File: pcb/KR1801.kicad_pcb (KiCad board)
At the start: 2 copper layers, 1 part, among them U1 К1801ВМ1

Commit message: ECB
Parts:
- added J1: ECB, Connector_DIN:DIN41612_R_3x32_Male_Horizontal_THT, F.Cu at (216.3, 60.0)
- added MH1: MountingHole_2.7mm_M2.5_DIN965, MountingHole:MountingHole_2.7mm_M2.5_DIN965, F.Cu at (65.2, 55.0)
- added MH2: MountingHole_2.7mm_M2.5_DIN965, MountingHole:MountingHole_2.7mm_M2.5_DIN965, F.Cu at (65.2, 143.9)
- moved U1 21.8 mm to (134.4, 111.9), turned to 90 degrees
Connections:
- U1 pad 1: unconnected-(U1-CLC-Pad1) -> CLC
- U1 pad 21: unconnected-(U1-GND-Pad21) -> GND
- U1 pad 29: unconnected-(U1-~{DCLO}-Pad29) -> ~{DCLO}
- U1 pad 30: unconnected-(U1-~{ACLO}-Pad30) -> ~{ACLO}
- U1 pad 34: unconnected-(U1-~{INIT}-Pad34) -> ~{INIT}
- U1 pad 42: unconnected-(U1-VCC-Pad42) -> VCC
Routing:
- net VCC: track 0.00 -> 104.2 mm
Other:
- board outline added: 160 x 100 mm
- board text added: "Mounting holes are optional Keepout areas are for for guide rails"

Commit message: 3D models
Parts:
- moved U1 2.99 mm to (136.4, 109.8)
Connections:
- J1 pad a11: unconnected-(J1-Pin_a11-Pada11) -> ~{DMR}
- J1 pad a22: unconnected-(J1-Pin_a22-Pada22) -> ~{RPLY}
- J1 pad a31: unconnected-(J1-Pin_a31-Pada31) -> ~{DMGO}
- J1 pad b25: unconnected-(J1-Pin_b25-Padb25) -> ~{IAKO}
- J1 pad c21: unconnected-(J1-Pin_c21-Padc21) -> ~{VIRQ}
- J1 pad c22: unconnected-(J1-Pin_c22-Padc22) -> ~{DOUT}
- J1 pad c24: unconnected-(J1-Pin_c24-Padc24) -> ~{DIN}
- J1 pad c25: unconnected-(J1-Pin_c25-Padc25) -> ~{IRQ1}
- U1 pad 2: unconnected-(U1-~{SACK}-Pad2) -> ~{SACK}
- U1 pad 31: unconnected-(U1-~{IRQ1}-Pad31) -> ~{IRQ1}
- U1 pad 32: unconnected-(U1-IRQ2-Pad32) -> ~{IRQ2}
- U1 pad 33: unconnected-(U1-IRQ3-Pad33) -> ~{IRQ3}
- U1 pad 35: unconnected-(U1-VIRQ-Pad35) -> ~{VIRQ}
- U1 pad 36: unconnected-(U1-IAKO-Pad36) -> ~{IAKO}
- U1 pad 37: unconnected-(U1-~{DOUT}-Pad37) -> ~{DOUT}
- U1 pad 38: unconnected-(U1-~{DIN}-Pad38) -> ~{DIN}
- U1 pad 39: unconnected-(U1-~{RPLY}-Pad39) -> ~{RPLY}
- U1 pad 4: unconnected-(U1-~{DMGO}-Pad4) -> ~{DMGO}
- U1 pad 40: unconnected-(U1-~{WTBT}-Pad40) -> ~{WTBT}
- U1 pad 41: unconnected-(U1-~{SYNC}-Pad41) -> ~{ALE}
- U1 pad 5: unconnected-(U1-~{DMR}-Pad5) -> ~{DMR}
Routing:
- net VCC: track 104.2 -> 0.00 mm

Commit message: random placement test
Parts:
- added R1: R, Resistor_SMD:R_0603_1608Metric_Pad0.98x0.95mm_HandSolder, F.Cu at (135.0, 123.7)
- added R10: 0R, Resistor_SMD:R_0603_1608Metric_Pad0.98x0.95mm_HandSolder, F.Cu at (145.8, 72.4)
- added R11: 0R, Resistor_SMD:R_0603_1608Metric_Pad0.98x0.95mm_HandSolder, F.Cu at (140.0, 72.3)
- added R12: R, Resistor_SMD:R_0603_1608Metric_Pad0.98x0.95mm_HandSolder, F.Cu at (172.3, 59.4)
- added R13: R, Resistor_SMD:R_0603_1608Metric_Pad0.98x0.95mm_HandSolder, F.Cu at (143.0, 72.3)
- added R14: R, Resistor_SMD:R_0603_1608Metric_Pad0.98x0.95mm_HandSolder, F.Cu at (137.6, 72.3)
- added R15: R, Resistor_SMD:R_0603_1608Metric_Pad0.98x0.95mm_HandSolder, F.Cu at (132.2, 123.9)
- added R2: R, Resistor_SMD:R_0603_1608Metric_Pad0.98x0.95mm_HandSolder, F.Cu at (137.5, 123.7)
- added R3: R, Resistor_SMD:R_0603_1608Metric_Pad0.98x0.95mm_HandSolder, F.Cu at (139.8, 123.7)
- added R4: R, Resistor_SMD:R_0603_1608Metric_Pad0.98x0.95mm_HandSolder, F.Cu at (142.8, 123.7)
- added R5: R, Resistor_SMD:R_0603_1608Metric_Pad0.98x0.95mm_HandSolder, F.Cu at (145.1, 123.6)
- added R6: R, Resistor_SMD:R_0603_1608Metric_Pad0.98x0.95mm_HandSolder, F.Cu at (149.4, 72.3)
- added R7: R, Resistor_SMD:R_0603_1608Metric_Pad0.98x0.95mm_HandSolder, F.Cu at (147.0, 123.6)
- added R8: 0R, Resistor_SMD:R_0603_1608Metric_Pad0.98x0.95mm_HandSolder, F.Cu at (129.8, 123.8)
- added R9: 0R, Resistor_SMD:R_0603_1608Metric_Pad0.98x0.95mm_HandSolder, F.Cu at (127.6, 123.8)
- added U2: 74LS573, Package_SO:SOIC-20W_7.5x12.8mm_P1.27mm, F.Cu at (180.2, 80.8)
- added U3: 74LS573, Package_SO:SOIC-20W_7.5x12.8mm_P1.27mm, F.Cu at (180.8, 108.8)
- added U4: 74LS245, Package_SO:SOIC-20W_7.5x12.8mm_P1.27mm, F.Cu at (193.0, 65.4)
- added U5: 74LS245, Package_SO:SOIC-20W_7.5x12.8mm_P1.27mm, F.Cu at (193.2, 94.0)
- moved U1 29.0 mm to (150.6, 84.5), turned to -90 degrees
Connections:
- J1 pad a18: unconnected-(J1-A14-Pada18) -> A14
- J1 pad a2: unconnected-(J1-D5-Pada2) -> DB5
- J1 pad a29: unconnected-(J1-A13-Pada29) -> A13
- J1 pad a3: unconnected-(J1-D6-Pada3) -> DB6
- J1 pad a30: unconnected-(J1-A9-Pada30) -> A9
- J1 pad a4: unconnected-(J1-D3-Pada4) -> DB3
- J1 pad a5: unconnected-(J1-D4-Pada5) -> DB4
- J1 pad a6: unconnected-(J1-A2-Pada6) -> A2
- J1 pad a7: unconnected-(J1-A4-Pada7) -> A4
- J1 pad a8: unconnected-(J1-A5-Pada8) -> A5
- J1 pad a9: unconnected-(J1-A6-Pada9) -> A6
- J1 pad b10: unconnected-(J1-D12-Padb10) -> DB12
- J1 pad b11: unconnected-(J1-D13-Padb11) -> DB13
- J1 pad b12: unconnected-(J1-D14-Padb12) -> DB14
- J1 pad b13: unconnected-(J1-D15-Padb13) -> DB15
- J1 pad b6: unconnected-(J1-D8-Padb6) -> DB8
- J1 pad b7: unconnected-(J1-D9-Padb7) -> DB9
- J1 pad b8: unconnected-(J1-D10-Padb8) -> DB10
- J1 pad b9: unconnected-(J1-D11-Padb9) -> DB11
- J1 pad c14: unconnected-(J1-D1-Padc14) -> DB1
- J1 pad c17: unconnected-(J1-A11-Padc17) -> A11
- J1 pad c18: unconnected-(J1-A10-Padc18) -> A10
- J1 pad c2: unconnected-(J1-D0-Padc2) -> DB0
- J1 pad c20: ~{ACLO} -> ~{NMI}
- J1 pad c26: ~{INIT} -> ~{DCLO}
- J1 pad c27: unconnected-(J1-A12-Padc27) -> A12
- J1 pad c28: unconnected-(J1-A15-Padc28) -> A15
- J1 pad c3: unconnected-(J1-D7-Padc3) -> DB7
- J1 pad c4: unconnected-(J1-D2-Padc4) -> DB2
- J1 pad c5: unconnected-(J1-A0-Padc5) -> A0
- J1 pad c6: unconnected-(J1-A3-Padc6) -> A3
- J1 pad c7: unconnected-(J1-A1-Padc7) -> A1
- J1 pad c8: unconnected-(J1-A8-Padc8) -> A8
- J1 pad c9: unconnected-(J1-A7-Padc9) -> A7
- U1 pad 10: unconnected-(U1-AD1-Pad10) -> AD1
- U1 pad 11: unconnected-(U1-AD2-Pad11) -> AD2
- U1 pad 12: unconnected-(U1-AD3-Pad12) -> AD3
- U1 pad 13: unconnected-(U1-AD4-Pad13) -> AD4
- U1 pad 14: unconnected-(U1-AD5-Pad14) -> AD5
- U1 pad 15: unconnected-(U1-AD6-Pad15) -> AD6
- U1 pad 16: unconnected-(U1-AD7-Pad16) -> AD7
- U1 pad 17: unconnected-(U1-AD8-Pad17) -> AD8
- U1 pad 18: unconnected-(U1-AD9-Pad18) -> AD9
- U1 pad 19: unconnected-(U1-AD10-Pad19) -> AD10
- U1 pad 20: unconnected-(U1-AD11-Pad20) -> AD11
- U1 pad 22: unconnected-(U1-AD12-Pad22) -> AD12
- U1 pad 23: unconnected-(U1-AD13-Pad23) -> AD13
- U1 pad 24: unconnected-(U1-AD14-Pad24) -> AD14
- U1 pad 25: unconnected-(U1-AD15-Pad25) -> AD15
- U1 pad 26: (no net) -> Net-(U1-~{PA1})
- U1 pad 27: unconnected-(U1-Pad27) -> Net-(U1-~{PA0})
- U1 pad 28: unconnected-(U1-Pad28) -> AB.OE
- U1 pad 3: unconnected-(U1-Pad3) -> Net-(U1-~{DMGI})
- U1 pad 34: ~{INIT} -> ~{DCLO}
- U1 pad 6: unconnected-(U1-Pad6) -> Net-(U1-~{SP})
- U1 pad 7: unconnected-(U1-SEL1-Pad7) -> ~{SEL1}
- U1 pad 8: unconnected-(U1-SEL2-Pad8) -> ~{SEL2}
- U1 pad 9: unconnected-(U1-AD0-Pad9) -> AD0

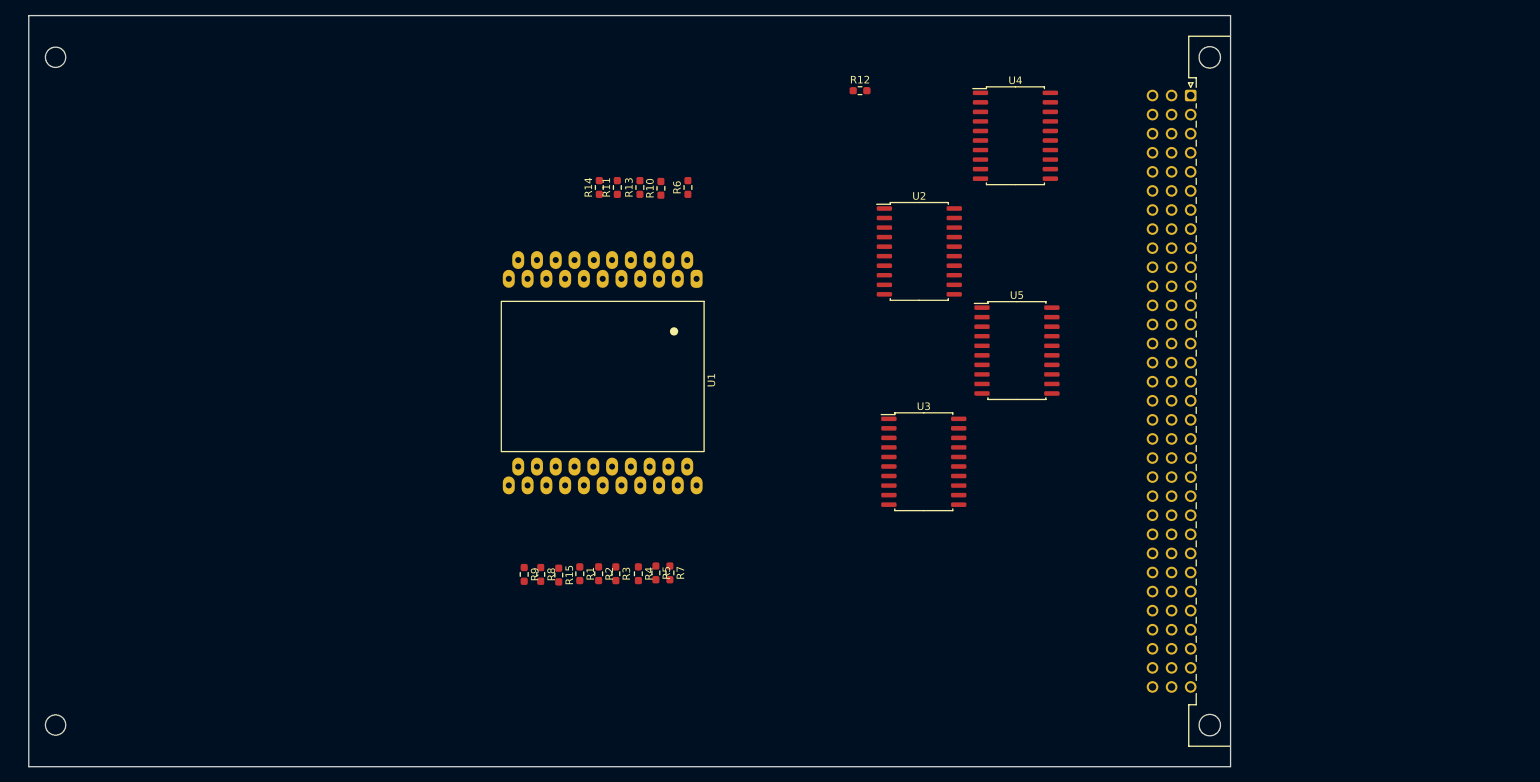
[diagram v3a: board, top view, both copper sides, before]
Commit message: most of the glue logic and controls
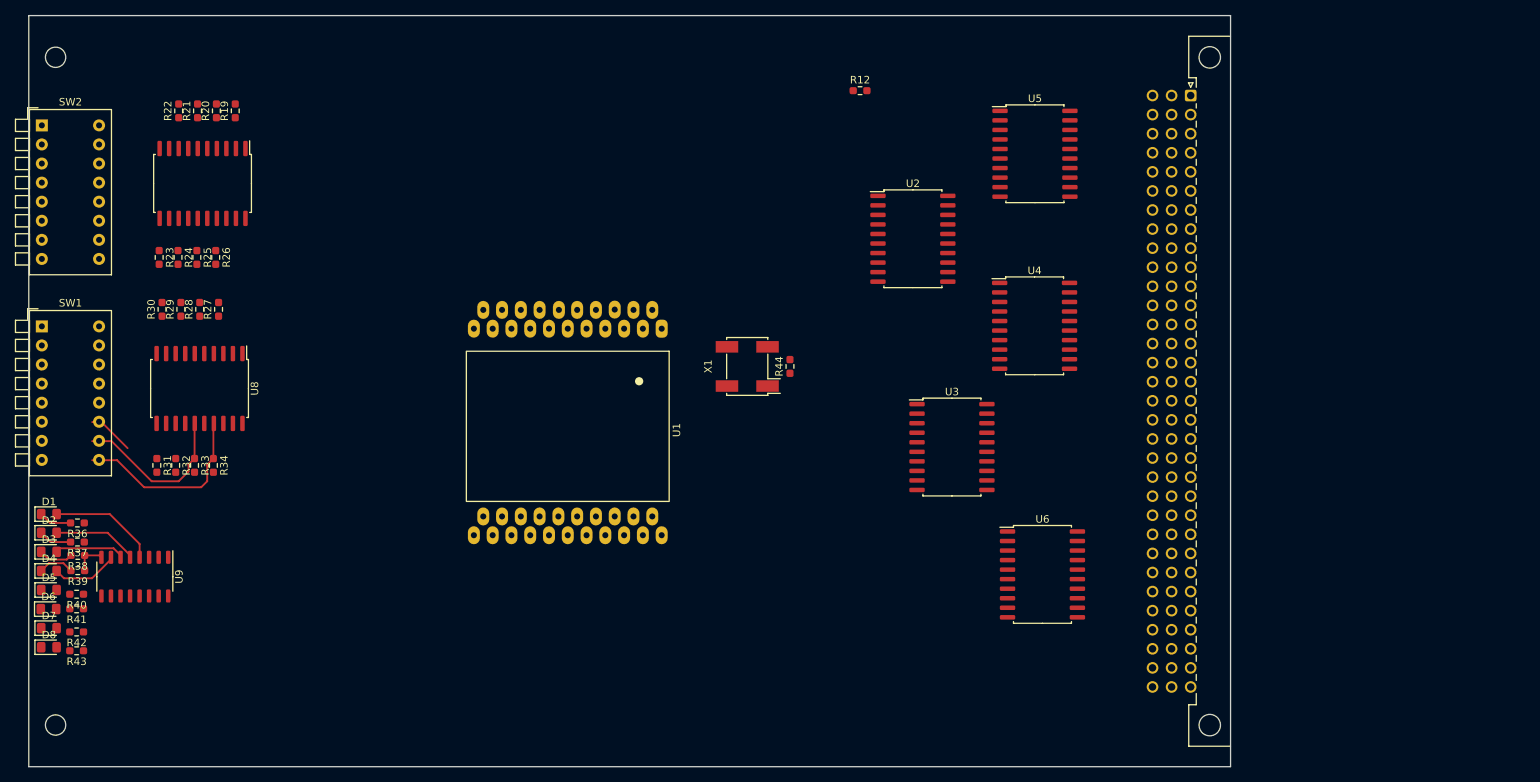
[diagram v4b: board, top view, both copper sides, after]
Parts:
- removed R1, R13, R14, R15, R2, R3, R4, R5, R6, R7: R, Resistor_SMD:R_0603_1608Metric_Pad0.98x0.95mm_HandSolder
- removed R10, R11, R8, R9: 0R, Resistor_SMD:R_0603_1608Metric_Pad0.98x0.95mm_HandSolder
- added D1: LED, LED_SMD:LED_0805_2012Metric_Pad1.15x1.40mm_HandSolder, F.Cu at (64.3, 115.8)
- added D2: LED, LED_SMD:LED_0805_2012Metric_Pad1.15x1.40mm_HandSolder, F.Cu at (64.3, 118.3)
- added D3: LED, LED_SMD:LED_0805_2012Metric_Pad1.15x1.40mm_HandSolder, F.Cu at (64.3, 120.8)
- added D4: LED, LED_SMD:LED_0805_2012Metric_Pad1.15x1.40mm_HandSolder, F.Cu at (64.3, 123.3)
- added D5: LED, LED_SMD:LED_0805_2012Metric_Pad1.15x1.40mm_HandSolder, F.Cu at (64.3, 125.9)
- added D6: LED, LED_SMD:LED_0805_2012Metric_Pad1.15x1.40mm_HandSolder, F.Cu at (64.3, 128.4)
- added D7: LED, LED_SMD:LED_0805_2012Metric_Pad1.15x1.40mm_HandSolder, F.Cu at (64.3, 131.0)
- added D8: LED, LED_SMD:LED_0805_2012Metric_Pad1.15x1.40mm_HandSolder, F.Cu at (64.3, 133.5)
- added R19: R, Resistor_SMD:R_0603_1608Metric_Pad0.98x0.95mm_HandSolder, F.Cu at (89.1, 62.1)
- added R20: R, Resistor_SMD:R_0603_1608Metric_Pad0.98x0.95mm_HandSolder, F.Cu at (86.6, 62.1)
- added R21: R, Resistor_SMD:R_0603_1608Metric_Pad0.98x0.95mm_HandSolder, F.Cu at (84.1, 62.1)
- added R22: R, Resistor_SMD:R_0603_1608Metric_Pad0.98x0.95mm_HandSolder, F.Cu at (81.6, 62.1)
- added R23: R, Resistor_SMD:R_0603_1608Metric_Pad0.98x0.95mm_HandSolder, F.Cu at (79.0, 81.6)
- added R24: R, Resistor_SMD:R_0603_1608Metric_Pad0.98x0.95mm_HandSolder, F.Cu at (81.5, 81.6)
- added R25: R, Resistor_SMD:R_0603_1608Metric_Pad0.98x0.95mm_HandSolder, F.Cu at (84.0, 81.6)
- added R26: R, Resistor_SMD:R_0603_1608Metric_Pad0.98x0.95mm_HandSolder, F.Cu at (86.5, 81.6)
- added R27: R, Resistor_SMD:R_0603_1608Metric_Pad0.98x0.95mm_HandSolder, F.Cu at (86.9, 88.5)
- added R28: R, Resistor_SMD:R_0603_1608Metric_Pad0.98x0.95mm_HandSolder, F.Cu at (84.4, 88.5)
- added R29: R, Resistor_SMD:R_0603_1608Metric_Pad0.98x0.95mm_HandSolder, F.Cu at (81.9, 88.5)
- added R30: R, Resistor_SMD:R_0603_1608Metric_Pad0.98x0.95mm_HandSolder, F.Cu at (79.4, 88.5)
- added R31: R, Resistor_SMD:R_0603_1608Metric_Pad0.98x0.95mm_HandSolder, F.Cu at (78.7, 109.3)
- added R32: R, Resistor_SMD:R_0603_1608Metric_Pad0.98x0.95mm_HandSolder, F.Cu at (81.2, 109.3)
- added R33: R, Resistor_SMD:R_0603_1608Metric_Pad0.98x0.95mm_HandSolder, F.Cu at (83.7, 109.3)
- added R34: R, Resistor_SMD:R_0603_1608Metric_Pad0.98x0.95mm_HandSolder, F.Cu at (86.2, 109.3)
- added R36: RLED, Resistor_SMD:R_0603_1608Metric_Pad0.98x0.95mm_HandSolder, F.Cu at (68.1, 117.0)
- added R37: RLED, Resistor_SMD:R_0603_1608Metric_Pad0.98x0.95mm_HandSolder, F.Cu at (68.1, 119.5)
- added R38: RLED, Resistor_SMD:R_0603_1608Metric_Pad0.98x0.95mm_HandSolder, F.Cu at (68.2, 121.3)
- added R39: RLED, Resistor_SMD:R_0603_1608Metric_Pad0.98x0.95mm_HandSolder, F.Cu at (68.2, 123.3)
- added R40: RLED, Resistor_SMD:R_0603_1608Metric_Pad0.98x0.95mm_HandSolder, F.Cu at (68.0, 126.4)
- added R41: RLED, Resistor_SMD:R_0603_1608Metric_Pad0.98x0.95mm_HandSolder, F.Cu at (68.0, 128.4)
- added R42: RLED, Resistor_SMD:R_0603_1608Metric_Pad0.98x0.95mm_HandSolder, F.Cu at (68.0, 131.5)
- added R43: RLED, Resistor_SMD:R_0603_1608Metric_Pad0.98x0.95mm_HandSolder, F.Cu at (68.0, 134.0)
- added R44: NPR, Resistor_SMD:R_0603_1608Metric_Pad0.98x0.95mm_HandSolder, F.Cu at (163.0, 96.1)
- added SW1: Reset Vector, Button_Switch_THT:SW_DIP_SPSTx08_Piano_10.8x21.88mm_W7.62mm_P2.54mm, F.Cu at (63.4, 90.8)
- added SW2: Opts, Button_Switch_THT:SW_DIP_SPSTx08_Piano_10.8x21.88mm_W7.62mm_P2.54mm, F.Cu at (63.4, 64.0)
- added U6: 74AHC273, Package_SO:SOIC-20W_7.5x12.8mm_P1.27mm, F.Cu at (196.6, 123.8)
- added U7: 74LS240, Package_SO:SOIC-20W_7.5x12.8mm_P1.27mm, F.Cu at (84.8, 71.8)
- added U8: 74LS240, Package_SO:SOIC-20W_7.5x12.8mm_P1.27mm, F.Cu at (84.4, 99.0)
- added U9: 74LS259, Package_SO:SO-16_3.9x9.9mm_P1.27mm, F.Cu at (75.8, 124.1)
- added X1: ~, Oscillator:Oscillator_SMD_Fordahl_DFAS2-4Pin_7.3x5.1mm_HandSoldering, F.Cu at (157.3, 96.1)
- moved U5 26.3 mm to (195.6, 67.8)
- moved U4 25.4 mm to (195.6, 90.7)
- moved U1 8.10 mm to (145.9, 91.1)
- moved U3 4.23 mm to (184.6, 106.8)
- moved U2 1.89 mm to (179.3, 79.1)
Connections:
- J1 pad a22: ~{RPLY} -> ~{RDY}
- J1 pad b28: unconnected-(J1-~{DS0}-Padb28) -> Net-(J1-~{DS0})
- J1 pad b29: unconnected-(J1-~{DS1}-Padb29) -> ~{DS1}
- J1 pad c24: ~{DIN} -> DT/~{R}
- J1 pad c25: ~{IRQ1} -> ~{HALT}
- R12 pad 1: ~{NMI} -> ~{DMR}
- U1 pad 28: AB.OE -> ~{BEN}
- U1 pad 38: ~{DIN} -> DT/~{R}
- U1 pad 6: Net-(U1-~{SP}) -> ~{SP}
- U2 pad 1: unconnected-(U2-OE-Pad1) -> ~{BEN}
- U2 pad 10: unconnected-(U2-GND-Pad10) -> GND
- U2 pad 11: unconnected-(U2-Load-Pad11) -> ~{ALE}
- U2 pad 20: unconnected-(U2-VCC-Pad20) -> VCC
- U3 pad 1: unconnected-(U3-OE-Pad1) -> ~{BEN}
- U3 pad 10: unconnected-(U3-GND-Pad10) -> GND
- U3 pad 11: unconnected-(U3-Load-Pad11) -> ~{ALE}
- U3 pad 20: unconnected-(U3-VCC-Pad20) -> VCC
- U4 pad 1: unconnected-(U4-A->B-Pad1) -> DT/~{R}
- U4 pad 11: DB7 -> DB15
- U4 pad 12: DB6 -> DB14
- U4 pad 13: DB5 -> DB13
- U4 pad 14: DB4 -> DB12
- U4 pad 15: DB3 -> DB11
- U4 pad 16: DB2 -> DB10
- U4 pad 17: DB1 -> DB9
- U4 pad 18: DB0 -> DB8
- U4 pad 19: unconnected-(U4-CE-Pad19) -> ~{BEN}
- U4 pad 2: AD0 -> AD8
- U4 pad 3: AD1 -> AD9
- U4 pad 4: AD2 -> AD10
- U4 pad 5: AD3 -> AD11
- U4 pad 6: AD4 -> AD12
- U4 pad 7: AD5 -> AD13
- U4 pad 8: AD6 -> AD14
- U4 pad 9: AD7 -> AD15
- U5 pad 1: unconnected-(U5-A->B-Pad1) -> DT/~{R}
- U5 pad 11: DB15 -> DB7
- U5 pad 12: DB14 -> DB6
- U5 pad 13: DB13 -> DB5
- U5 pad 14: DB12 -> DB4
- U5 pad 15: DB11 -> DB3
- U5 pad 16: DB10 -> DB2
- U5 pad 17: DB9 -> DB1
- U5 pad 18: DB8 -> DB0
- U5 pad 19: unconnected-(U5-CE-Pad19) -> ~{BEN}
- U5 pad 2: AD8 -> AD0
- U5 pad 3: AD9 -> AD1
- U5 pad 4: AD10 -> AD2
- U5 pad 5: AD11 -> AD3
- U5 pad 6: AD12 -> AD4
- U5 pad 7: AD13 -> AD5
- U5 pad 8: AD14 -> AD6
- U5 pad 9: AD15 -> AD7
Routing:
- net DR15: track 0.00 -> 25.2 mm
- net DR14: track 0.00 -> 22.3 mm
- net Net-(D1-A): track 0.00 -> 14.5 mm
- net Net-(D2-A): track 0.00 -> 11.3 mm
- net Net-(D3-A): track 0.00 -> 9.36 mm
- net Net-(D4-A): track 0.00 -> 8.96 mm
- net DR13: track 0.00 -> 6.16 mm
- net Net-(D4-K): track 0.00 -> 4.79 mm
- net Net-(D3-K): track 0.00 -> 4.61 mm
- net Net-(D2-K): track 0.00 -> 4.42 mm
- net Net-(D1-K): track 0.00 -> 4.40 mm
- net GND: track 0.00 -> 4.38 mm

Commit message: final logic, gal, 3D
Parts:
- removed MH1, MH2: MountingHole_2.7mm_M2.5_DIN965, MountingHole:MountingHole_2.7mm_M2.5_DIN965
- added U10: GAL16V8, Package_LCC:PLCC-20, F.Cu at (110.8, 108.8)
- J1: footprint Connector_DIN:DIN41612_R_3x32_Male_Horizontal_THT -> Connector_DIN:DIN41612_C_3x32_Male_Horizontal_THT
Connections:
- J1 pad c20: ~{NMI} -> ~{ACLO}
- J1 pad c26: ~{DCLO} -> ~{INIT}
- U1 pad 34: ~{DCLO} -> ~{INIT}
- U4 pad 19: ~{BEN} -> ~{DEN}
- U5 pad 19: ~{BEN} -> ~{DEN}
- U6 pad 1: VCC -> ~{DCLO}
- U6 pad 3: ~{NMI} -> ~{ACLO}

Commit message: /init
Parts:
- added D10: NMI, LED_SMD:LED_0805_2012Metric_Pad1.15x1.40mm_HandSolder, F.Cu at (250.6, 104.0)
- added D9: DCLO, LED_SMD:LED_0805_2012Metric_Pad1.15x1.40mm_HandSolder, F.Cu at (250.6, 101.0)
- added R1: 0R, Resistor_SMD:R_0603_1608Metric_Pad0.98x0.95mm_HandSolder, F.Cu at (250.4, 90.7)
- added R10: 0R, Resistor_SMD:R_0603_1608Metric_Pad0.98x0.95mm_HandSolder, F.Cu at (244.0, 103.2)
- added R11: R, Resistor_SMD:R_0603_1608Metric_Pad0.98x0.95mm_HandSolder, F.Cu at (244.0, 105.7)
- added R13: R, Resistor_SMD:R_0603_1608Metric_Pad0.98x0.95mm_HandSolder, F.Cu at (244.0, 108.2)
- added R14: R, Resistor_SMD:R_0603_1608Metric_Pad0.98x0.95mm_HandSolder, F.Cu at (254.7, 90.7)
- added R16: 0R, Resistor_SMD:R_0603_1608Metric_Pad0.98x0.95mm_HandSolder, F.Cu at (254.7, 93.2)
- added R17: 0R, Resistor_SMD:R_0603_1608Metric_Pad0.98x0.95mm_HandSolder, F.Cu at (254.7, 95.7)
- added R18: 0R, Resistor_SMD:R_0603_1608Metric_Pad0.98x0.95mm_HandSolder, F.Cu at (244.0, 110.8)
- added R2: 0R, Resistor_SMD:R_0603_1608Metric_Pad0.98x0.95mm_HandSolder, F.Cu at (250.4, 93.2)
- added R3: R, Resistor_SMD:R_0603_1608Metric_Pad0.98x0.95mm_HandSolder, F.Cu at (250.4, 95.7)
- added R35: RLED, Resistor_SMD:R_0603_1608Metric_Pad0.98x0.95mm_HandSolder, F.Cu at (254.7, 98.2)
- added R4: R, Resistor_SMD:R_0603_1608Metric_Pad0.98x0.95mm_HandSolder, F.Cu at (244.0, 90.7)
- added R45: R, Resistor_SMD:R_0603_1608Metric_Pad0.98x0.95mm_HandSolder, F.Cu at (259.1, 90.7)
- added R46: RLED, Resistor_SMD:R_0603_1608Metric_Pad0.98x0.95mm_HandSolder, F.Cu at (259.1, 93.2)
- added R48: 0R, Resistor_SMD:R_0603_1608Metric_Pad0.98x0.95mm_HandSolder, F.Cu at (259.1, 95.7)
- added R49: 0R, Resistor_SMD:R_0603_1608Metric_Pad0.98x0.95mm_HandSolder, F.Cu at (259.1, 99.6)
- added R5: R, Resistor_SMD:R_0603_1608Metric_Pad0.98x0.95mm_HandSolder, F.Cu at (244.0, 93.2)
- added R6: 0R, Resistor_SMD:R_0603_1608Metric_Pad0.98x0.95mm_HandSolder, F.Cu at (250.4, 98.2)
- added R7: R, Resistor_SMD:R_0603_1608Metric_Pad0.98x0.95mm_HandSolder, F.Cu at (244.0, 95.7)
- added R8: 0R, Resistor_SMD:R_0603_1608Metric_Pad0.98x0.95mm_HandSolder, F.Cu at (244.0, 98.2)
- added R9: 0R, Resistor_SMD:R_0603_1608Metric_Pad0.98x0.95mm_HandSolder, F.Cu at (244.0, 100.7)
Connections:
- U10 pad 13: Net-(U10-IO7) -> FAIL.LED
- U10 pad 14: FAIL.LED -> NMI.LED
- U10 pad 15: NMI.LED -> Net-(U10-IO5)

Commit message: full? schematics
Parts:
- removed R1, R10, R16, R17, R18, R2, R48, R49, R6, R8, R9: 0R, Resistor_SMD:R_0603_1608Metric_Pad0.98x0.95mm_HandSolder
- removed R11, R12, R13, R14, R3, R4, R45, R5, R7: R, Resistor_SMD:R_0603_1608Metric_Pad0.98x0.95mm_HandSolder
- removed R35, R46: RLED, Resistor_SMD:R_0603_1608Metric_Pad0.98x0.95mm_HandSolder
- added SW3: NMI, Button_Switch_THT:SW_SPST_Omron_B3F-315x_Angled, F.Cu at (65.4, 132.1)
- added SW4: RESET, Button_Switch_THT:SW_SPST_Omron_B3F-315x_Angled, F.Cu at (65.5, 142.5)
- J1: value ECB -> Eurocard UNIBUS
- U2, U3: value 74LS573 -> 74HC564
- U4, U5: value 74LS245 -> 74HC640
- moved D10 188.5 mm to (64.8, 135.1)
- moved D9 187.4 mm to (64.7, 124.7)
- moved U10 34.8 mm to (130.4, 137.6)
- moved U6 15.6 mm to (182.4, 130.4)
- moved U4 14.7 mm to (182.4, 97.3)
- moved D1 13.3 mm to (64.8, 102.5)
- moved D3 13.3 mm to (64.8, 107.5)
- moved D5 13.3 mm to (64.8, 112.6)
- moved D6 13.3 mm to (64.7, 115.1)
- moved R36 13.3 mm to (68.6, 103.7)
- moved R38 13.3 mm to (68.6, 108.0)
- moved R40 13.3 mm to (68.5, 113.2)
- moved R41 13.3 mm to (68.5, 115.1)
- moved R43 13.3 mm to (68.5, 120.7)
- moved D2 13.3 mm to (64.8, 105.0)
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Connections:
- J1 pad b29: ~{DS1} -> Net-(J1-~{DS1})
- J1 pad c20: ~{ACLO} -> ~{NMI}
- U10 pad 12: Net-(U10-IO8) -> ALE
- U10 pad 18: ~{REG} -> ~{DS1}
- U10 pad 4: ~{SEL1} -> Net-(U10-I4)
- U10 pad 5: ~{SEL2} -> ~{WTBT}
- U10 pad 9: Net-(U10-I9) -> ~{ALE}
- U2 pad 11: ~{ALE} -> ALE
- U3 pad 11: ~{ALE} -> ALE
- U6 pad 3: ~{ACLO} -> ~{NMI}
- U8 pad 1: ~{REG} -> ~{SEL1}
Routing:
- net DB8: track 0.00 -> 39.4 mm, vias 0 -> 1
- net DB9: track 0.00 -> 38.8 mm, vias 0 -> 1
- net DB10: track 0.00 -> 37.3 mm, vias 0 -> 1
- net DB11: track 0.00 -> 36.1 mm, vias 0 -> 1
- net DB12: track 0.00 -> 33.4 mm
- net DB13: track 0.00 -> 32.9 mm
- net A6: track 0.00 -> 32.4 mm, vias 0 -> 2
- net DB14: track 0.00 -> 32.4 mm
- net DB15: track 0.00 -> 31.9 mm
- net A4: track 0.00 -> 31.7 mm
- net A2: track 0.00 -> 31.7 mm
- net A5: track 0.00 -> 31.2 mm
- net A3: track 0.00 -> 30.4 mm, vias 0 -> 2
- net A0: track 0.00 -> 26.7 mm, vias 0 -> 1
- net A7: track 0.00 -> 26.1 mm
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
